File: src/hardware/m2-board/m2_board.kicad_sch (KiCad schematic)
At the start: 17 parts, among them J1 TYPE-C-31-M-12, SW1 TS-1088R-02026, SW2 TS-1088R-02026, U1 ESP32-C3-WROOM-02-N4, U2 SHT30-DIS-B10KS, U3 ME6211C33M5G-N

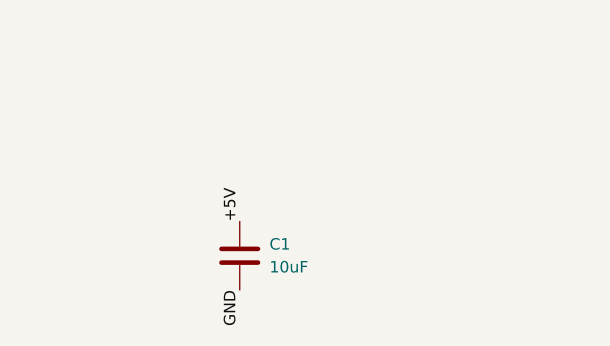
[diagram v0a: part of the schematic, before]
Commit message: fix: restore M2 ERC power semantics
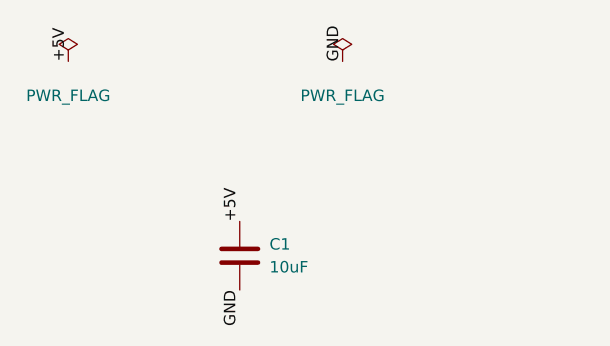
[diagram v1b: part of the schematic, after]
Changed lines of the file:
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@@
 		)
 	)
+	(symbol (lib_id "power:PWR_FLAG") (at 15.24 15.24 0) (unit 1) (pin "1") (property "Reference" "#FLG01" (at 15.24 17.145 0) (effects (font (size 1.27 1.27)) (hide yes))) (instances (project "noname" (path "/a1dbe1c3-f1f0-496b-b2c7-2a432ea67147" (reference "#FLG01") (unit 1))))
+	(property "Value" "PWR_FLAG" (at 15.24 19.05 0) (effects (font (size 1.27 1.27))))
+	(property "Footprint" "" (at 15.24 15.24 0) (effects (font (size 1.27 1.27)) (hide yes))))
+	(symbol (lib_id "power:PWR_FLAG") (at 45.72 15.24 0) (unit 1) (pin "1") (property "Reference" "#FLG02" (at 45.72 17.145 0) (effects (font (size 1.27 1.27)) (hide yes))) (instances (project "noname" (path "/a1dbe1c3-f1f0-496b-b2c7-2a432ea67147" (reference "#FLG02") (unit 1))))
+	(property "Value" "PWR_FLAG" (at 45.72 19.05 0) (effects (font (size 1.27 1.27))))
+	(property "Footprint" "" (at 45.72 15.24 0) (effects (font (size 1.27 1.27)) (hide yes))))
+	(label "+5V" (at 15.24 15.24 90) (effects (font (size 1.27 1.27)) (justify left bottom)))
+	(label "GND" (at 45.72 15.24 90) (effects (font (size 1.27 1.27)) (justify left bottom)))
 	(symbol (lib_id "Device:C") (at 34.29 36.83 0) (unit 1) (pin "1") (pin "2") (property "Reference" "C1" (at 37.592 35.56 0) (effects (font (size 1.27 1.27)) (justify left))) (instances (project "noname" (path "/a1dbe1c3-f1f0-496b-b2c7-2a432ea67147" (reference "C1") (unit 1))))
 	(property "Value" "10uF" (at 37.592 38.1 0) (effects (font (size 1.27 1.27)) (justify left)))

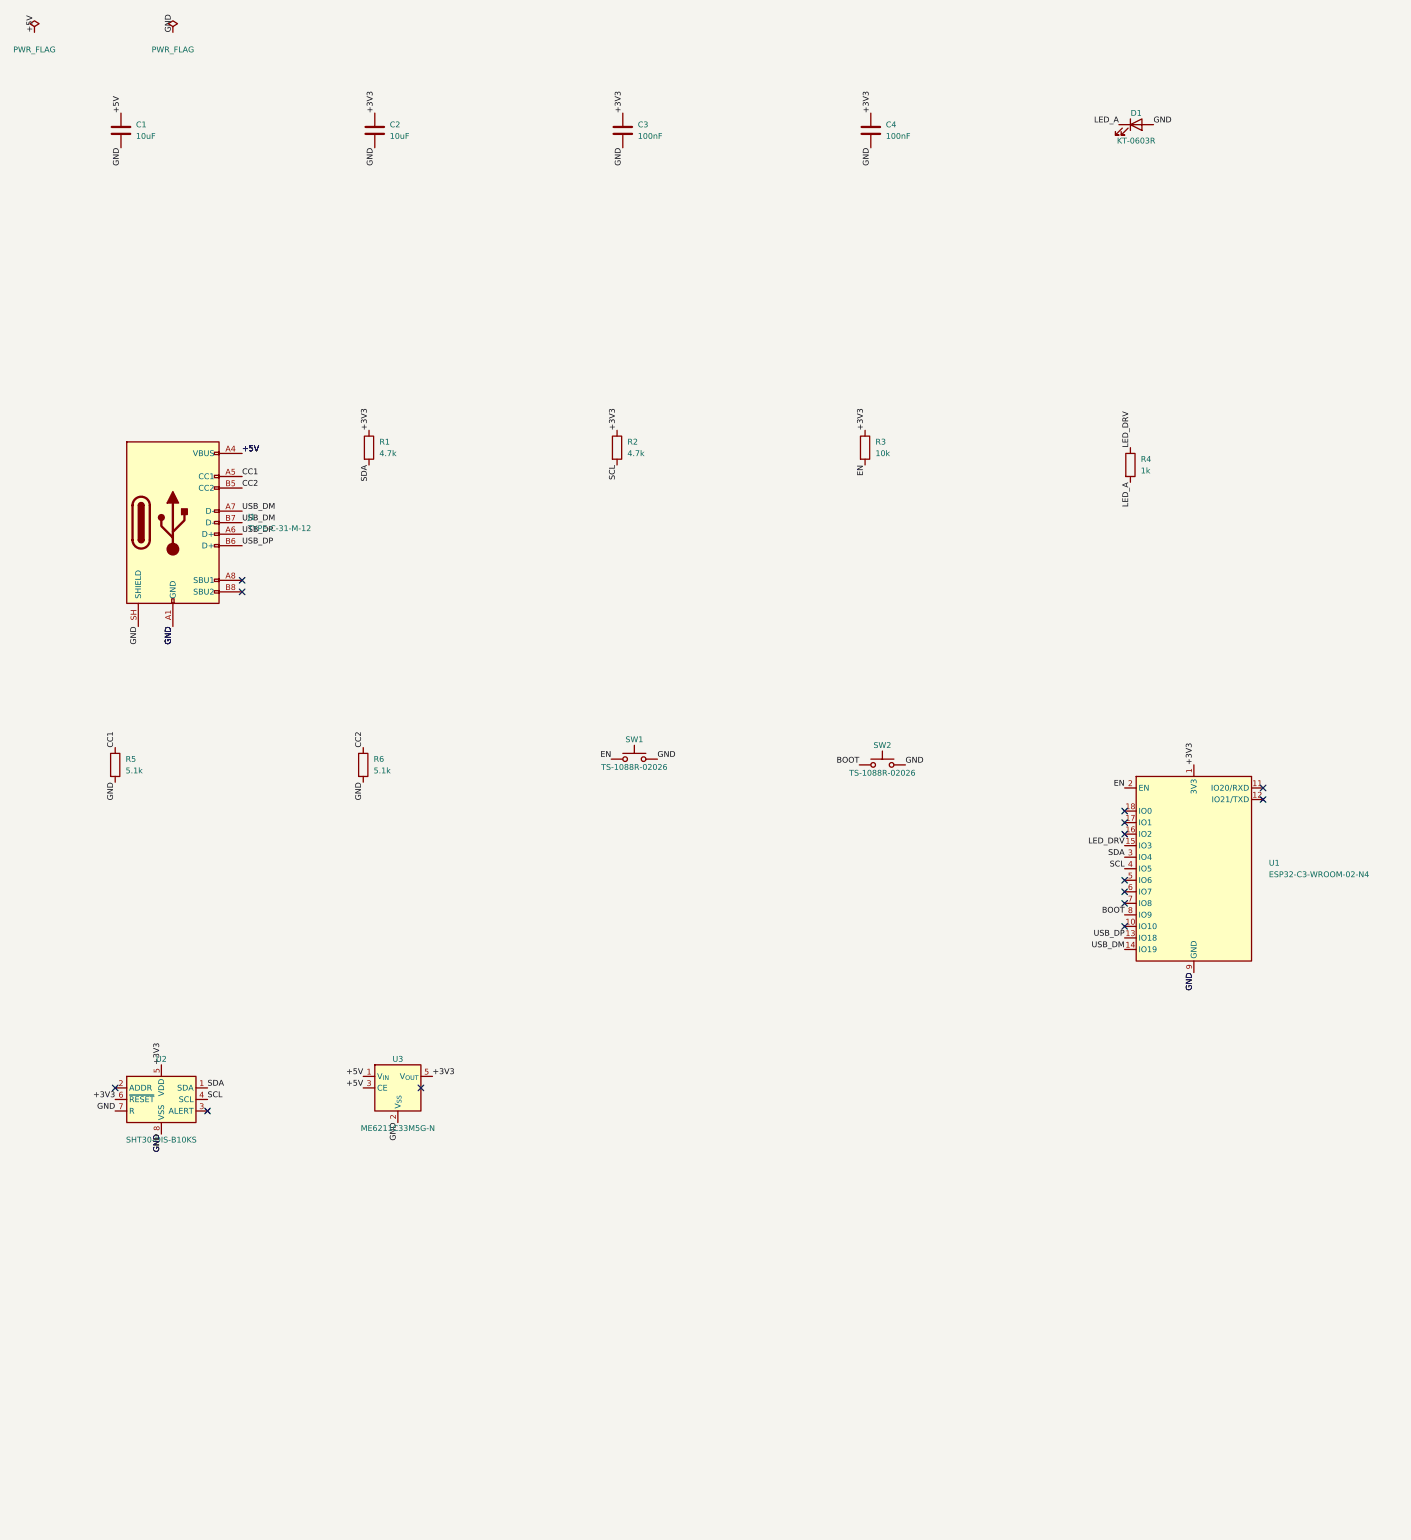
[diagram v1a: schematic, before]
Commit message: fix(schematic): repair M2 datasheet semantics [AI-20260830-001]
- regenerate the canonical schematic and ops with locked akcli 0.21.0
- encode USB polarity/series resistors, SHT30 strap/NC intent, EN RC, and GPIO9 pull-up
- preserve fail-closed release state until PCB artifacts are reconciled and re-reviewed
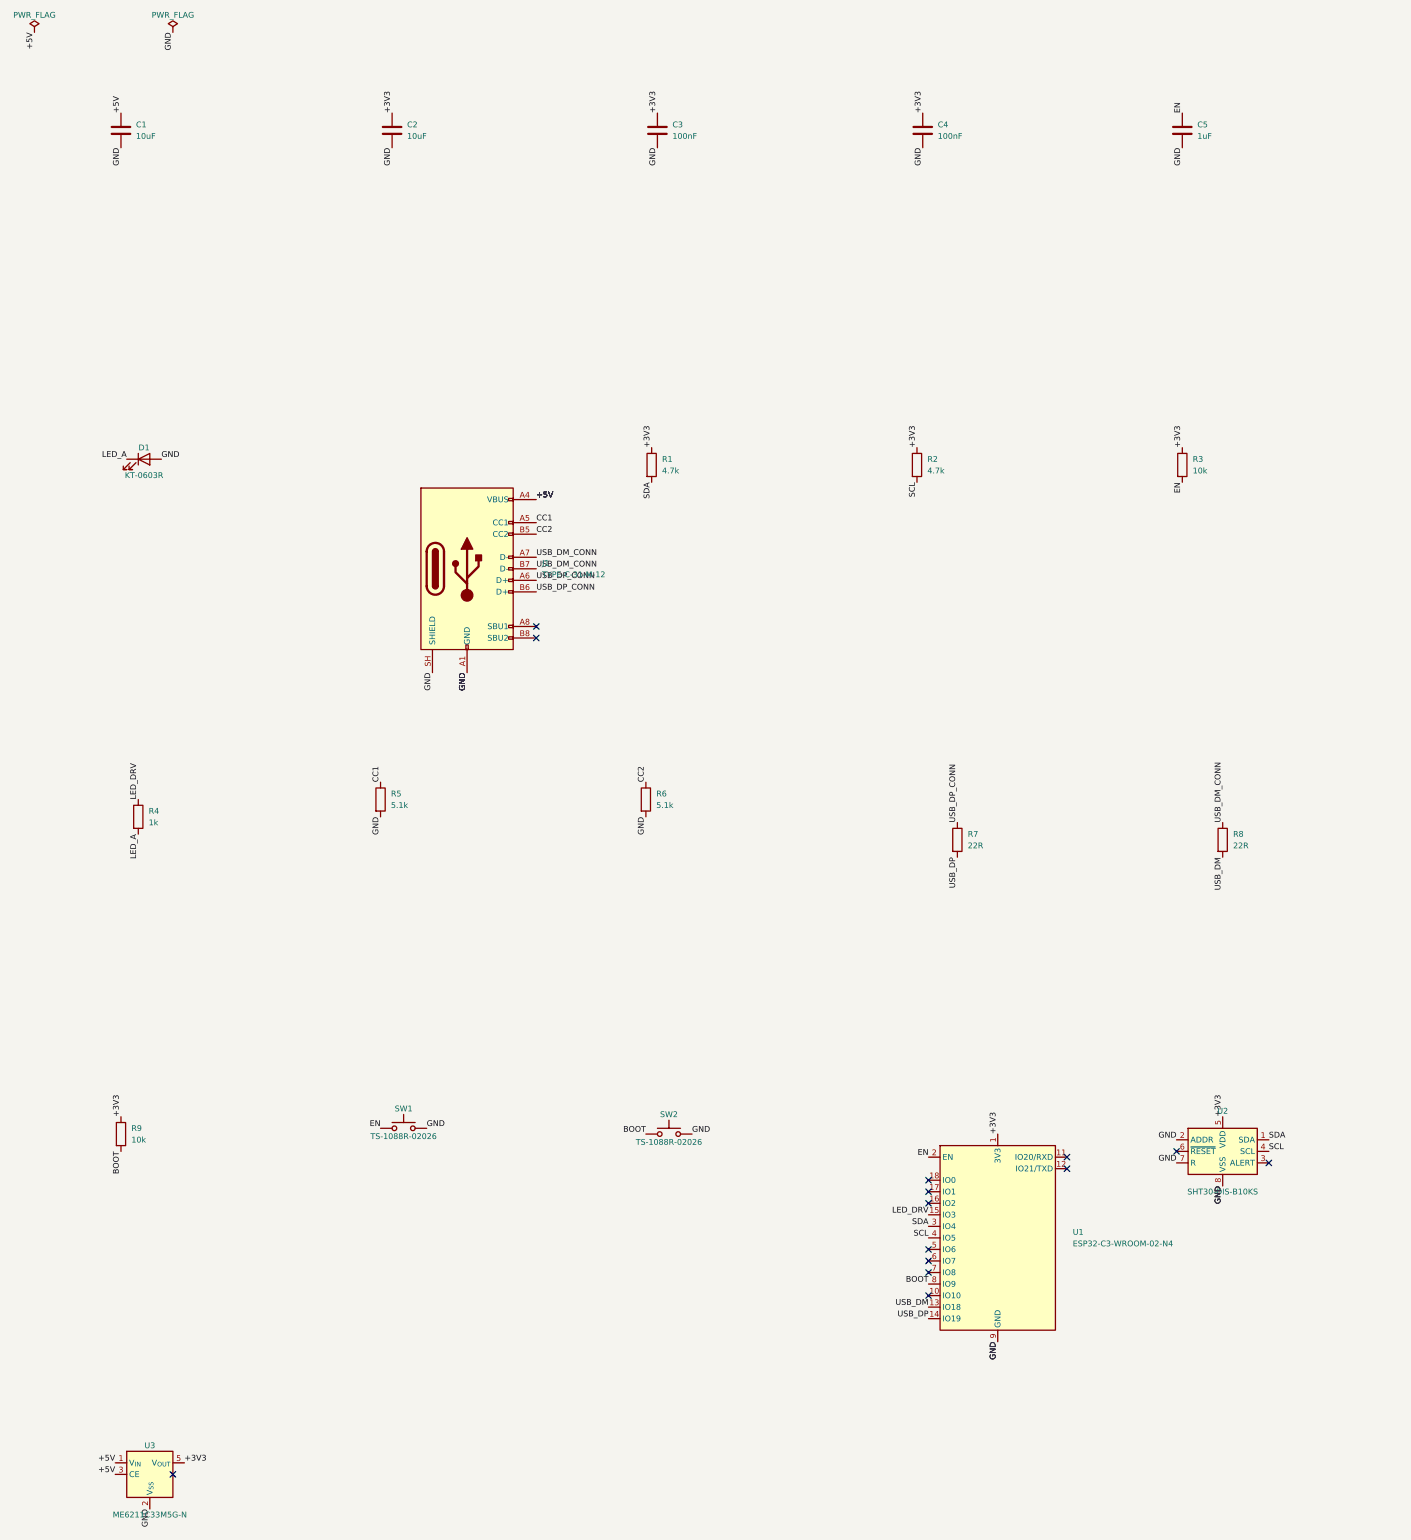
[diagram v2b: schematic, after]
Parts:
- added C5: 1uF, Capacitor_SMD:C_0603_1608Metric, symbol Device:C
- added R7, R8: 22R, Resistor_SMD:R_0603_1608Metric, symbol Device:R
- added R9: 10k, Resistor_SMD:R_0603_1608Metric, symbol Device:R
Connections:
- net +3V3: now also R9.1; no longer U2.6 (~{RESET})
- net BOOT: now also R9.2
- net EN: now also C5.1
- net GND: now also U2.2 (ADDR), C5.2
- net USB_DM: now also U1.13 (IO18), R8.2; no longer J1.A7 (D-), J1.B7 (D-), U1.14 (IO19)
- net USB_DP: now also U1.14 (IO19), R7.2; no longer J1.A6 (D+), J1.B6 (D+), U1.13 (IO18)
- new net USB_DM_CONN: J1.A7 (D-), J1.B7 (D-), R8.1
- new net USB_DP_CONN: J1.A6 (D+), J1.B6 (D+), R7.1
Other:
- moved on the sheet: C2, C3, C4, D1, J1, R1, R2, R3, R4, R5, R6, SW1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

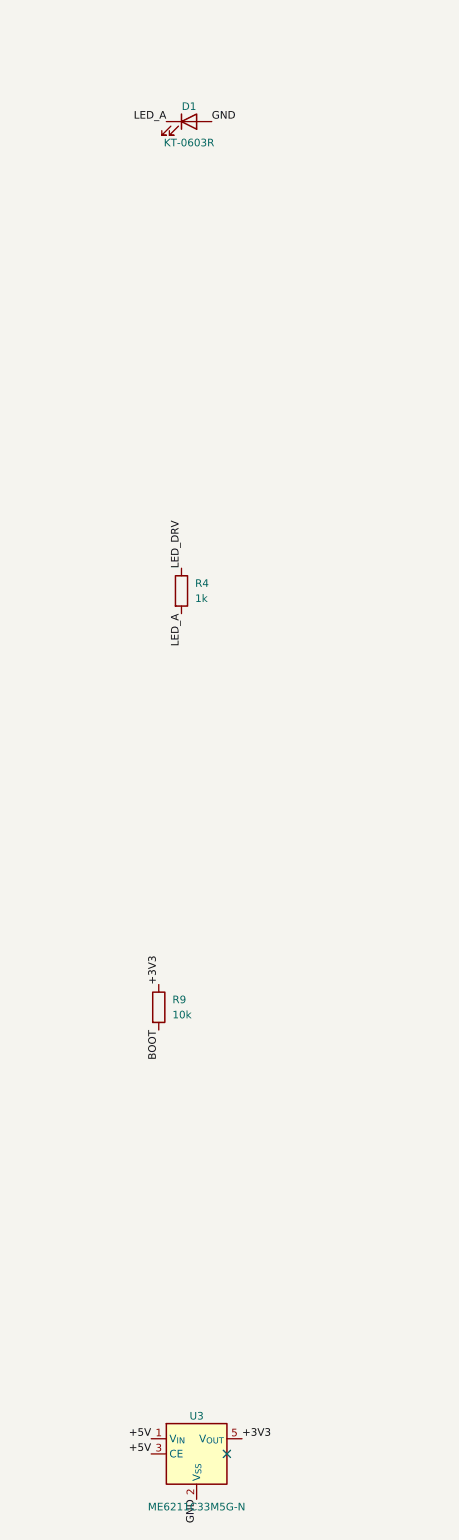
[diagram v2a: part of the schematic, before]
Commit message: fix(board): repair D1 LED polarity and swap U3 to C235316 [AI-20260831-007]
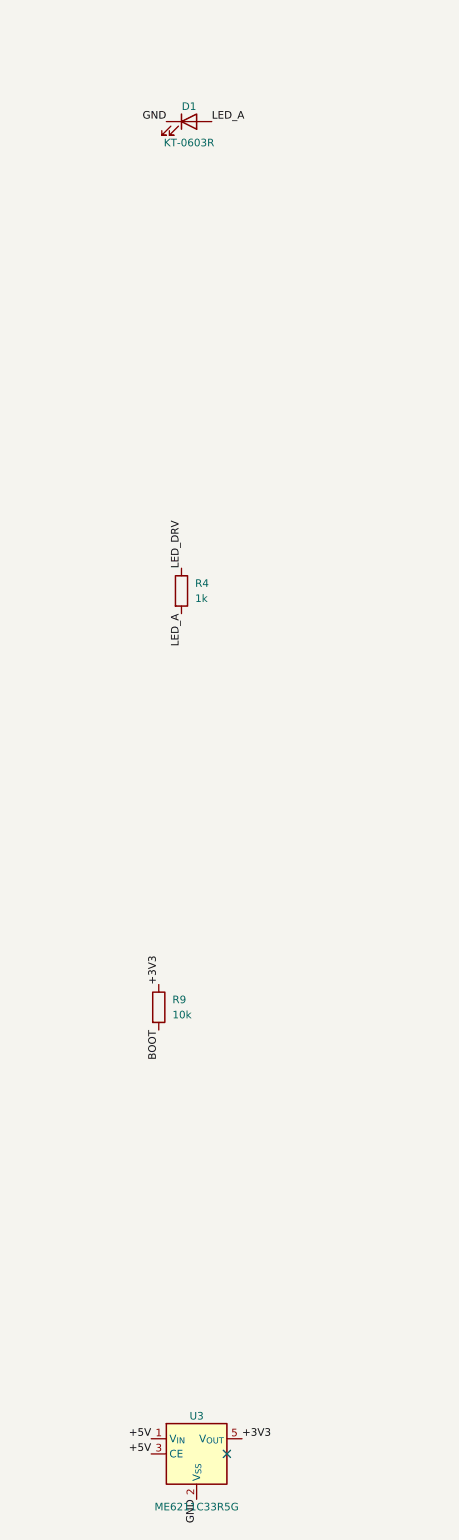
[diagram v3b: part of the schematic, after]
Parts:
- U3: value ME6211C33M5G-N -> ME6211C33R5G; footprint Package_TO_SOT_SMD:SOT-23-5 -> Package_TO_SOT_SMD:SOT-353
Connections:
- net GND: now also D1.1 (K); no longer D1.2 (A)
- net LED_A: now also D1.2 (A); no longer D1.1 (K)
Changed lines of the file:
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@@
 	(property "Value" "SHT30-DIS-B10KS" (at 276.86 270.51 0) (effects (font (size 1.27 1.27)))))
 	(symbol (lib_id "Regulator_Linear:ME6211C33M5") (at 40.64 332.74 0) (unit 1) (pin "1") (pin "2") (pin "3") (pin "4") (pin "5") (property "Reference" "U3" (at 40.64 326.39 0) (effects (font (size 1.27 1.27)))) (instances (project "noname" (path "/a1dbe1c3-f1f0-496b-b2c7-2a432ea67147" (reference "U3") (unit 1))))
-	(property "Value" "ME6211C33M5G-N" (at 40.64 341.63 0) (effects (font (size 1.27 1.27))))
-	(property "Footprint" "Package_TO_SOT_SMD:SOT-23-5" (at 40.64 332.74 0) (effects (font (size 1.27 1.27)) (hide yes))))
+	(property "Value" "ME6211C33R5G" (at 40.64 341.63 0) (effects (font (size 1.27 1.27))))
+	(property "Footprint" "Package_TO_SOT_SMD:SOT-353" (at 40.64 332.74 0) (effects (font (size 1.27 1.27)) (hide yes))))
 	(symbol (lib_id "power:PWR_FLAG") (at 15.24 15.24 0) (unit 1) (pin "1") (property "Reference" "#FLG01" (at 15.24 16.51 0) (effects (font (size 1.27 1.27)) (hide yes))) (instances (project "noname" (path "/a1dbe1c3-f1f0-496b-b2c7-2a432ea67147" (reference "#FLG01") (unit 1))))
 	(property "Value" "PWR_FLAG" (at 15.24 11.43 0) (effects (font (size 1.27 1.27)))))
@@
 	(label "GND" (at 210.82 40.64 270) (effects (font (size 1.27 1.27)) (justify right bottom)))
 	(label "GND" (at 267.97 40.64 270) (effects (font (size 1.27 1.27)) (justify right bottom)))
-	(label "GND" (at 43.18 109.22 0) (effects (font (size 1.27 1.27)) (justify left bottom)))
+	(label "LED_A" (at 43.18 109.22 0) (effects (font (size 1.27 1.27)) (justify left bottom)))
 	(label "GND" (at 110.49 156.21 270) (effects (font (size 1.27 1.27)) (justify right bottom)))
 	(label "GND" (at 110.49 156.21 270) (effects (font (size 1.27 1.27)) (justify right bottom)))
@@
 	(label "GND" (at 276.86 269.24 270) (effects (font (size 1.27 1.27)) (justify right bottom)))
 	(label "GND" (at 40.64 340.36 270) (effects (font (size 1.27 1.27)) (justify right bottom)))
-	(label "LED_A" (at 35.56 109.22 180) (effects (font (size 1.27 1.27)) (justify right bottom)))
+	(label "GND" (at 35.56 109.22 180) (effects (font (size 1.27 1.27)) (justify right bottom)))
 	(label "LED_A" (at 38.1 191.77 270) (effects (font (size 1.27 1.27)) (justify right bottom)))
 	(label "LED_DRV" (at 38.1 184.15 90) (effects (font (size 1.27 1.27)) (justify left bottom)))
